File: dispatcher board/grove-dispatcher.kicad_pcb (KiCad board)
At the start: 2 copper layers, 36 parts, among them P1 CONN_01X05, P10 CONN_01X06, P11 CONN_01X06, P12 CONN_01X06, P13 CONN_01X06, P14 CONN_01X06, P15 CONN_01X06, P16 CONN_01X06, P17 CONN_01X06, P18 CONN_01X06, P19 CONN_01X06, P2 CONN_01X06, P20 CONN_01X06, P3 CONN_01X05, P4 CONN_01X05, P5 CONN_01X05, P6 CONN_01X06, P7 CONN_01X06, P8 CONN_01X06, P9 CONN_01X06, U1 PICO_BUCK, U2 PICO_BUCK, U3 PICO_BUCK, U4 PICO_BUCK

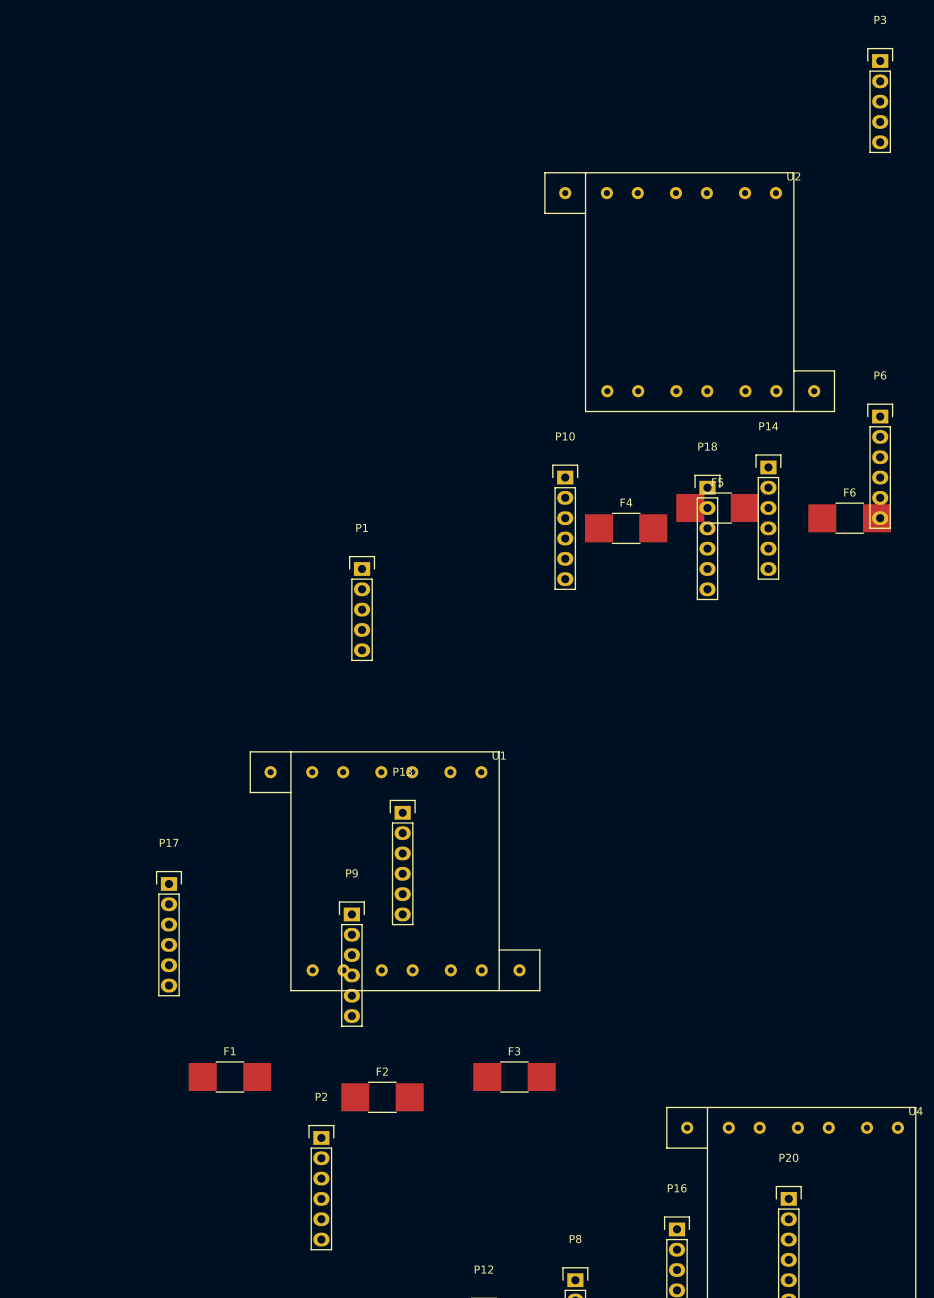
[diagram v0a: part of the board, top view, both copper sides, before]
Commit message: Some test placement on PCB
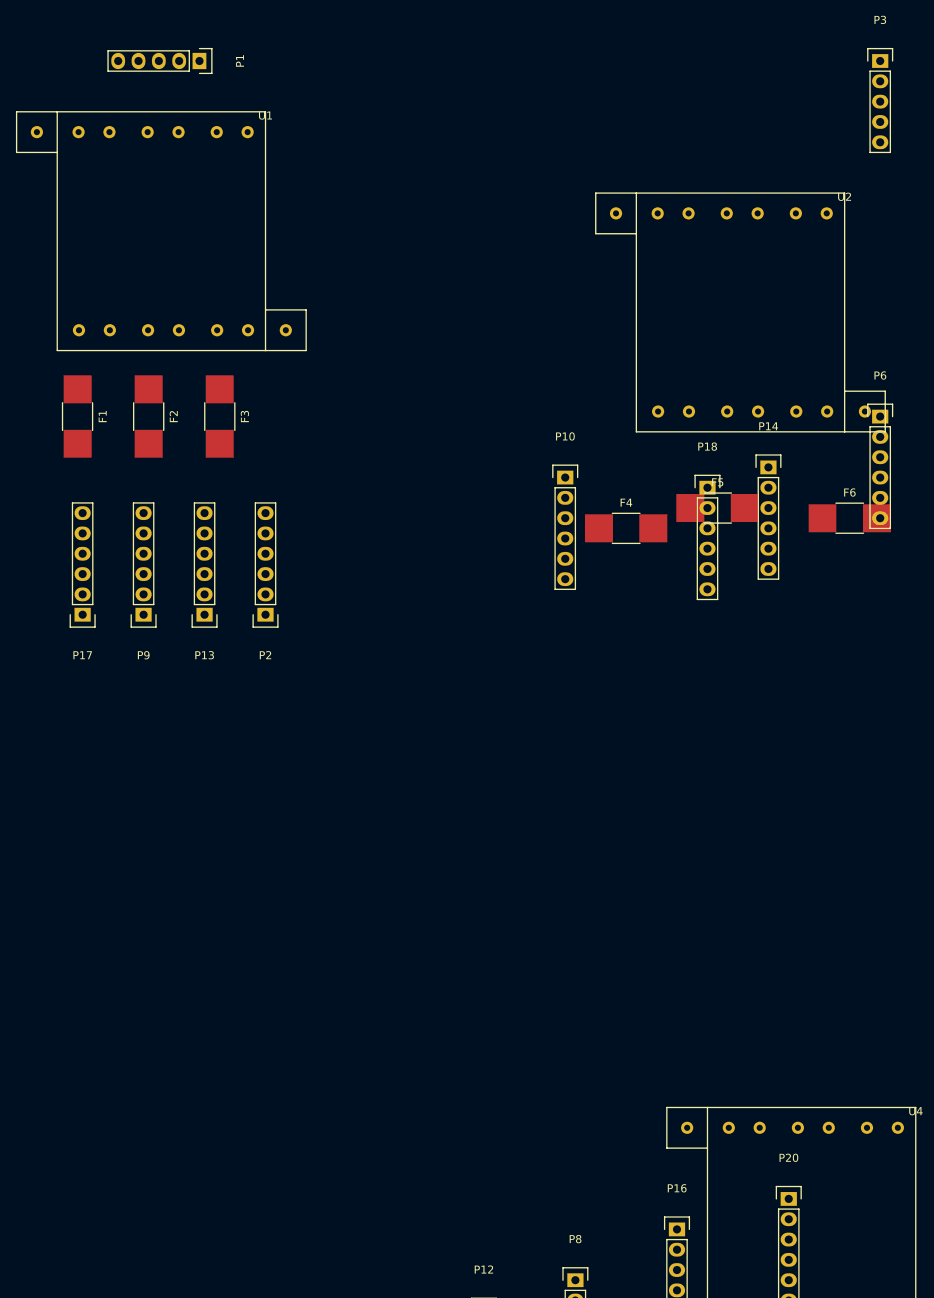
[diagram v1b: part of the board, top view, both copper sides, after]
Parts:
- moved F3 90.4 mm to (43.2, 61.0), turned to 270 degrees
- moved F2 90.0 mm to (34.3, 61.0), turned to 270 degrees
- moved U1 85.2 mm to (22.9, 22.9)
- moved F1 84.7 mm to (25.4, 61.0), turned to 270 degrees
- moved P1 66.7 mm to (40.6, 16.5), turned to 270 degrees
- moved P2 65.8 mm to (48.9, 85.7), turned to 180 degrees
- moved P9 45.6 mm to (33.7, 85.7), turned to 180 degrees
- moved P17 35.3 mm to (26.0, 85.7), turned to 180 degrees
- moved P13 35.0 mm to (41.3, 85.7), turned to 180 degrees
- moved U2 6.84 mm to (95.2, 33.0)

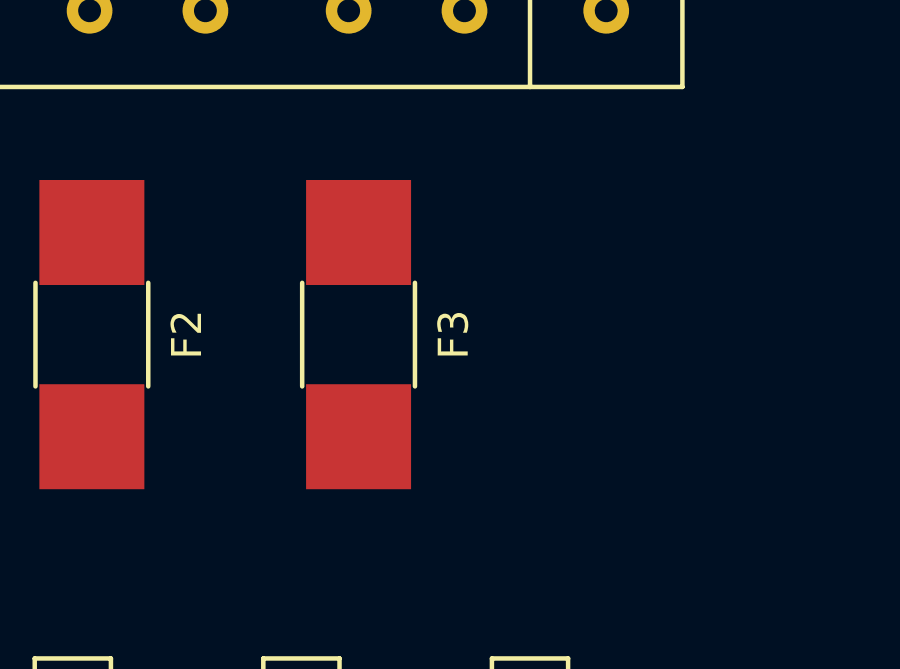
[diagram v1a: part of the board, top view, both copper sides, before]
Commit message: Some tweaks to the gitignore and pcb file
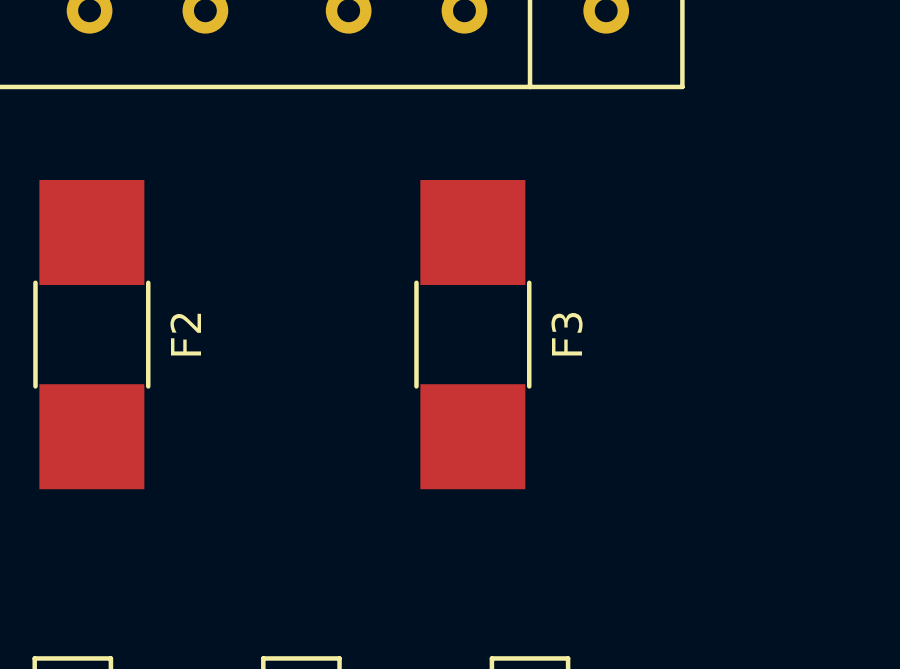
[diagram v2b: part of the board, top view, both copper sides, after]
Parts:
- moved F3 3.81 mm to (47.0, 61.0)
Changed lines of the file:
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@@
   )
   (module Resistors_SMD:R_1812_HandSoldering (layer F.Cu)
-    (at 43.18 60.96 270)
+    (at 46.99 60.96 270)
     (descr "Resistor SMD 1812, hand soldering, Panasonic (see ERJ12)")
     (tags "resistor 1812")

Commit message: First pass at routing this simple board
Conn for LED are spaced far enough apart to allow
for MTA connectors which are 0.3 inch or more thick
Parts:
- added R1: 0, Resistors_SMD:R_0805_HandSoldering, F.Cu at (119.4, 130.8)
- added R10: 0, Resistors_SMD:R_0805_HandSoldering, F.Cu at (182.2, 102.2)
- added R11: 0, Resistors_SMD:R_0805_HandSoldering, F.Cu at (182.2, 111.1)
- added R12: 0, Resistors_SMD:R_0805_HandSoldering, F.Cu at (182.2, 120.0)
- added R2: 0, Resistors_SMD:R_0805_HandSoldering, F.Cu at (119.4, 121.9)
- added R3: 0, Resistors_SMD:R_0805_HandSoldering, F.Cu at (119.4, 113.0)
- added R4: 0, Resistors_SMD:R_0805_HandSoldering, F.Cu at (119.4, 92.7)
- added R5: 0, Resistors_SMD:R_0805_HandSoldering, F.Cu at (119.4, 83.8)
- added R6: 0, Resistors_SMD:R_0805_HandSoldering, F.Cu at (119.4, 74.9)
- added R7: 0, Resistors_SMD:R_0805_HandSoldering, F.Cu at (182.2, 66.7)
- added R8: 0, Resistors_SMD:R_0805_HandSoldering, F.Cu at (182.2, 75.6)
- added R9: 0, Resistors_SMD:R_0805_HandSoldering, F.Cu at (182.2, 84.5)
- P11, P16, P6: value CONN_01X06 -> CONN_01X05; footprint Pin_Headers:Pin_Header_Straight_1x06 -> Pin_Headers:Pin_Header_Straight_1x05
- P3, P4, P5: value CONN_01X05 -> CONN_01X06; footprint Pin_Headers:Pin_Header_Straight_1x05 -> Pin_Headers:Pin_Header_Straight_1x06
- moved P16 134.2 mm to (226.7, 117.5), turned to 180 degrees
- moved U4 124.2 mm to (220.3, 103.5), turned to 270 degrees
- moved P8 123.7 mm to (169.5, 76.2), turned to 180 degrees
- moved P4 122.1 mm to (132.1, 114.3), turned to 180 degrees
- moved U1 121.6 mm to (81.3, 129.5), turned to 90 degrees
- moved F1 114.9 mm to (119.4, 127.0), turned to 0 degrees
- moved P17 111.8 mm to (132.1, 121.3), turned to 0 degrees
- moved P2 111.7 mm to (156.8, 114.3)
- moved P15 111.6 mm to (156.8, 83.2)
- moved P3 107.2 mm to (169.5, 114.3), turned to 180 degrees
- moved P12 105.5 mm to (132.1, 83.2)
- moved P13 103.5 mm to (144.8, 83.2), turned to 0 degrees
- moved F2 102.5 mm to (119.4, 118.1), turned to 0 degrees
- moved F10 100.3 mm to (182.2, 106.0), turned to 180 degrees
- moved P1 100.0 mm to (74.9, 110.5), turned to 0 degrees
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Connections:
- P1 pad 4: /V+ -> GND
- P1 pad 5: GND -> /V+
- P11 pad 1: Net-(F7-Pad2) -> Net-(P11-Pad1)
- P11 pad 3: Net-(F8-Pad2) -> Net-(P11-Pad3)
- P11 pad 4: Net-(P11-Pad4) -> GND
- P11 pad 5: Net-(F9-Pad2) -> Net-(P11-Pad5)
- P12 pad 1: Net-(F10-Pad2) -> Net-(F7-Pad2)
- P12 pad 3: Net-(F11-Pad2) -> Net-(F8-Pad2)
- P12 pad 5: Net-(F12-Pad2) -> Net-(F9-Pad2)
- P13 pad 1: Net-(F1-Pad2) -> Net-(F7-Pad2)
- P13 pad 2: Net-(P13-Pad2) -> Net-(P12-Pad2)
- P13 pad 3: Net-(F2-Pad2) -> Net-(F8-Pad2)
- P13 pad 4: Net-(P13-Pad4) -> Net-(P12-Pad4)
- P13 pad 5: Net-(F3-Pad2) -> Net-(F9-Pad2)
- P13 pad 6: Net-(P13-Pad6) -> Net-(P12-Pad6)
- P14 pad 1: Net-(F4-Pad2) -> Net-(F7-Pad2)
- P14 pad 2: Net-(P10-Pad2) -> Net-(P12-Pad2)
- P14 pad 3: Net-(F5-Pad2) -> Net-(F8-Pad2)
- P14 pad 4: Net-(P10-Pad4) -> Net-(P12-Pad4)
- P14 pad 5: Net-(F6-Pad2) -> Net-(F9-Pad2)
- P14 pad 6: Net-(P10-Pad6) -> Net-(P12-Pad6)
- P15 pad 2: Net-(P11-Pad2) -> Net-(P12-Pad2)
- P15 pad 4: Net-(P11-Pad4) -> Net-(P12-Pad4)
- P15 pad 6: Net-(P11-Pad6) -> Net-(P12-Pad6)
- P16 pad 1: Net-(F10-Pad2) -> Net-(P16-Pad1)
- P16 pad 2: Net-(P12-Pad2) -> Net-(P16-Pad2)
- P16 pad 3: Net-(F11-Pad2) -> Net-(P16-Pad3)
- P16 pad 4: Net-(P12-Pad4) -> GND
- P16 pad 5: Net-(F12-Pad2) -> Net-(P16-Pad5)
- P17 pad 1: Net-(F1-Pad2) -> Net-(F10-Pad2)
- P17 pad 2: Net-(P13-Pad2) -> Net-(P17-Pad2)
- P17 pad 3: Net-(F2-Pad2) -> Net-(F11-Pad2)
- P17 pad 4: Net-(P13-Pad4) -> Net-(P17-Pad4)
- P17 pad 5: Net-(F3-Pad2) -> Net-(F12-Pad2)
- P17 pad 6: Net-(P13-Pad6) -> Net-(P17-Pad6)
- P18 pad 1: Net-(F4-Pad2) -> Net-(F10-Pad2)
- P18 pad 2: Net-(P10-Pad2) -> Net-(P17-Pad2)
- P18 pad 3: Net-(F5-Pad2) -> Net-(F11-Pad2)
- P18 pad 4: Net-(P10-Pad4) -> Net-(P17-Pad4)
- P18 pad 5: Net-(F6-Pad2) -> Net-(F12-Pad2)
- P18 pad 6: Net-(P10-Pad6) -> Net-(P17-Pad6)
- P19 pad 1: Net-(F7-Pad2) -> Net-(F10-Pad2)
- P19 pad 2: Net-(P11-Pad2) -> Net-(P17-Pad2)
- P19 pad 3: Net-(F8-Pad2) -> Net-(F11-Pad2)
- P19 pad 4: Net-(P11-Pad4) -> Net-(P17-Pad4)
- P19 pad 5: Net-(F9-Pad2) -> Net-(F12-Pad2)
- P19 pad 6: Net-(P11-Pad6) -> Net-(P17-Pad6)
- P2 pad 2: Net-(P13-Pad2) -> Net-(P2-Pad2)
- P2 pad 4: Net-(P13-Pad4) -> Net-(P2-Pad4)
- P2 pad 6: Net-(P13-Pad6) -> Net-(P2-Pad6)
- P20 pad 2: Net-(P12-Pad2) -> Net-(P17-Pad2)
- P20 pad 4: Net-(P12-Pad4) -> Net-(P17-Pad4)
- P20 pad 6: Net-(P12-Pad6) -> Net-(P17-Pad6)
- P3 pad 1: Net-(P3-Pad1) -> Net-(F1-Pad2)
- P3 pad 2: Net-(P3-Pad2) -> Net-(P2-Pad2)
- P3 pad 3: Net-(P3-Pad3) -> Net-(F2-Pad2)
- P3 pad 4: /V+ -> Net-(P2-Pad4)
- P3 pad 5: GND -> Net-(F3-Pad2)
- P4 pad 1: Net-(P4-Pad1) -> Net-(F1-Pad2)
- P4 pad 2: Net-(P4-Pad2) -> Net-(P2-Pad2)
- P4 pad 3: Net-(P4-Pad3) -> Net-(F2-Pad2)
- P4 pad 4: /V+ -> Net-(P2-Pad4)
- P4 pad 5: GND -> Net-(F3-Pad2)
- P5 pad 1: Net-(P5-Pad1) -> Net-(F1-Pad2)
- P5 pad 2: Net-(P5-Pad2) -> Net-(P2-Pad2)
- P5 pad 3: Net-(P5-Pad3) -> Net-(F2-Pad2)
- P5 pad 4: /V+ -> Net-(P2-Pad4)
- P5 pad 5: GND -> Net-(F3-Pad2)
- P6 pad 1: Net-(F4-Pad2) -> Net-(P6-Pad1)
- P6 pad 2: Net-(P10-Pad2) -> Net-(P6-Pad2)
- P6 pad 3: Net-(F5-Pad2) -> Net-(P6-Pad3)
- P6 pad 4: Net-(P10-Pad4) -> GND
- P6 pad 5: Net-(F6-Pad2) -> Net-(P6-Pad5)
- P7 pad 1: Net-(F7-Pad2) -> Net-(F4-Pad2)
- P7 pad 2: Net-(P11-Pad2) -> Net-(P10-Pad2)
- P7 pad 3: Net-(F8-Pad2) -> Net-(F5-Pad2)
- P7 pad 4: Net-(P11-Pad4) -> Net-(P10-Pad4)
- P7 pad 5: Net-(F9-Pad2) -> Net-(F6-Pad2)
- P7 pad 6: Net-(P11-Pad6) -> Net-(P10-Pad6)
- P8 pad 1: Net-(F10-Pad2) -> Net-(F4-Pad2)
- P8 pad 2: Net-(P12-Pad2) -> Net-(P10-Pad2)
- P8 pad 3: Net-(F11-Pad2) -> Net-(F5-Pad2)
- P8 pad 4: Net-(P12-Pad4) -> Net-(P10-Pad4)
- P8 pad 5: Net-(F12-Pad2) -> Net-(F6-Pad2)
- P8 pad 6: Net-(P12-Pad6) -> Net-(P10-Pad6)
- P9 pad 1: Net-(F1-Pad2) -> Net-(F4-Pad2)
- P9 pad 2: Net-(P13-Pad2) -> Net-(P10-Pad2)
- P9 pad 3: Net-(F2-Pad2) -> Net-(F5-Pad2)
- P9 pad 4: Net-(P13-Pad4) -> Net-(P10-Pad4)
- P9 pad 5: Net-(F3-Pad2) -> Net-(F6-Pad2)
- P9 pad 6: Net-(P13-Pad6) -> Net-(P10-Pad6)
- U1 pad 0: Net-(P1-Pad3) -> Net-(P1-Pad1)
- U1 pad 11: Net-(P13-Pad6) -> Net-(P2-Pad6)
- U1 pad 2: Net-(P1-Pad1) -> Net-(P1-Pad3)
- U1 pad 7: Net-(P13-Pad2) -> Net-(P2-Pad2)
- U1 pad 9: Net-(P13-Pad4) -> Net-(P2-Pad4)
- U2 pad 0: Net-(P3-Pad3) -> Net-(P6-Pad1)
- U2 pad 1: Net-(P3-Pad2) -> Net-(P6-Pad2)
- U2 pad 2: Net-(P3-Pad1) -> Net-(P6-Pad3)
- U2 pad 5: /V+ -> Net-(P6-Pad5)
- U3 pad 0: Net-(P4-Pad3) -> Net-(P11-Pad1)
- U3 pad 1: Net-(P4-Pad2) -> Net-(P11-Pad2)
- U3 pad 11: Net-(P11-Pad6) -> Net-(P12-Pad6)
- U3 pad 2: Net-(P4-Pad1) -> Net-(P11-Pad3)
- U3 pad 5: /V+ -> Net-(P11-Pad5)
- U3 pad 7: Net-(P11-Pad2) -> Net-(P12-Pad2)
- U3 pad 9: Net-(P11-Pad4) -> Net-(P12-Pad4)
- U4 pad 0: Net-(P5-Pad3) -> Net-(P16-Pad1)
- U4 pad 1: Net-(P5-Pad2) -> Net-(P16-Pad2)
- U4 pad 11: Net-(P12-Pad6) -> Net-(P17-Pad6)
- U4 pad 2: Net-(P5-Pad1) -> Net-(P16-Pad3)
- U4 pad 5: /V+ -> Net-(P16-Pad5)
- U4 pad 7: Net-(P12-Pad2) -> Net-(P17-Pad2)
- U4 pad 9: Net-(P12-Pad4) -> Net-(P17-Pad4)
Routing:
- net Net-(P17-Pad2): track 0.00 -> 71.8 mm
- net Net-(P2-Pad2): track 0.00 -> 70.4 mm
- net Net-(P12-Pad2): track 0.00 -> 69.7 mm
- net Net-(P10-Pad2): track 0.00 -> 69.7 mm
- net Net-(P17-Pad4): track 0.00 -> 67.9 mm
- net Net-(P2-Pad4): track 0.00 -> 66.9 mm
- net Net-(P10-Pad4): track 0.00 -> 66.9 mm
- net Net-(P10-Pad6): track 0.00 -> 65.8 mm
- net Net-(P12-Pad4): track 0.00 -> 65.7 mm
- net Net-(P17-Pad6): track 0.00 -> 63.7 mm
- net Net-(P2-Pad6): track 0.00 -> 62.7 mm
- net Net-(P12-Pad6): track 0.00 -> 62.7 mm
- net Net-(F10-Pad2): track 0.00 -> 61.2 mm
- net Net-(F7-Pad2): track 0.00 -> 60.8 mm
- net Net-(F4-Pad2): track 0.00 -> 60.2 mm
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- added copper zone on F.Cu, net GND
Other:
- board outline added: 158.8 x 77.5 mm

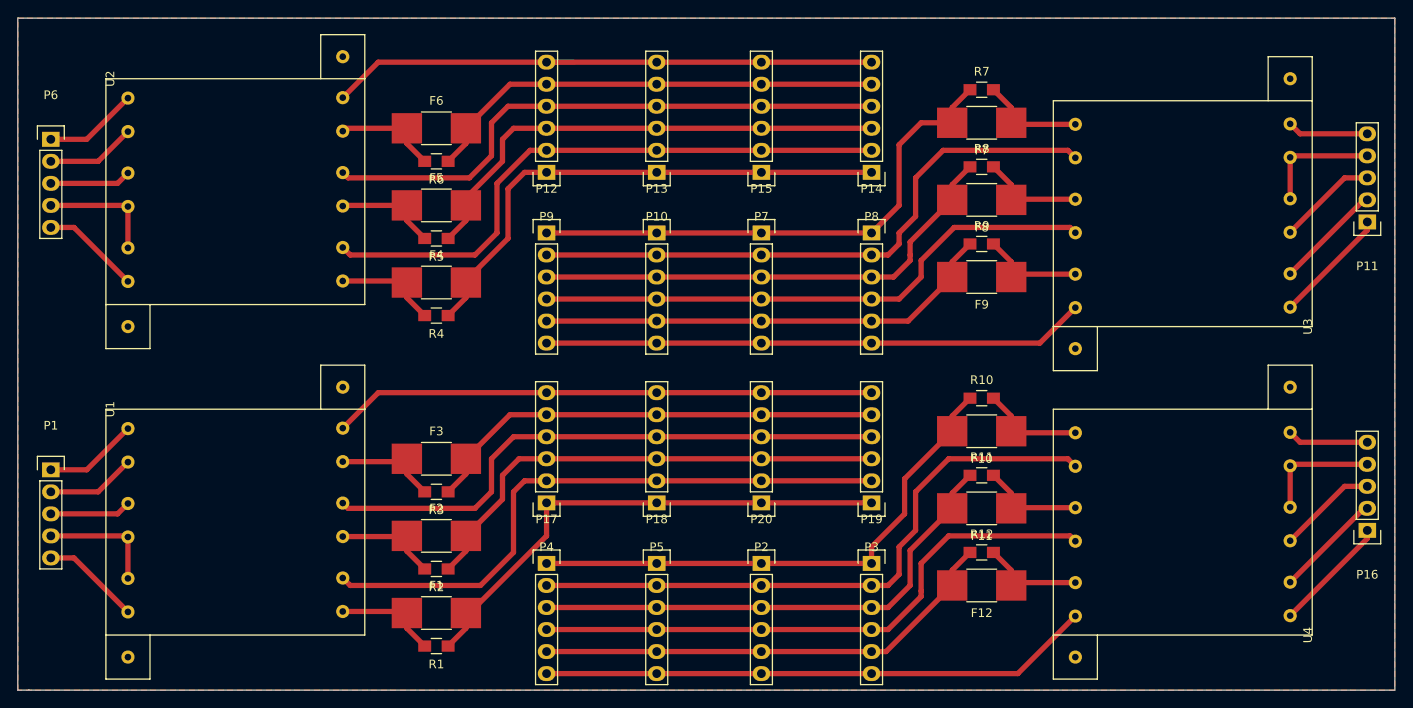
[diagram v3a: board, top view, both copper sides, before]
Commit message: Add some mounting holes
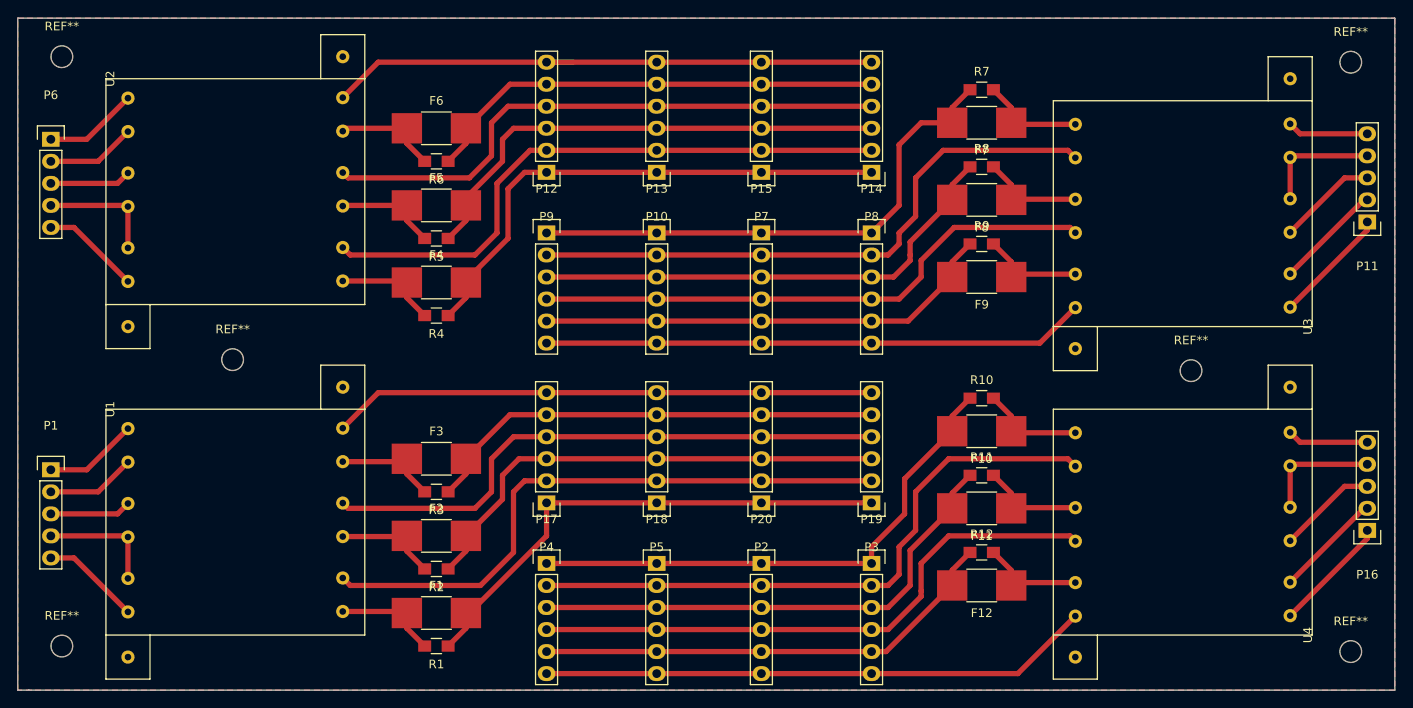
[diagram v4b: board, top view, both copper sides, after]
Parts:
- added REF**: MountingHole_2.5mm, Mounting_Holes:MountingHole_2.5mm, F.Cu at (224.8, 63.5)
- added REF**: MountingHole_2.5mm, Mounting_Holes:MountingHole_2.5mm, F.Cu at (206.4, 99.1)
- added REF**: MountingHole_2.5mm, Mounting_Holes:MountingHole_2.5mm, F.Cu at (224.8, 131.4)
- added REF**: MountingHole_2.5mm, Mounting_Holes:MountingHole_2.5mm, F.Cu at (76.2, 62.9)
- added REF**: MountingHole_2.5mm, Mounting_Holes:MountingHole_2.5mm, F.Cu at (95.9, 97.8)
- added REF**: MountingHole_2.5mm, Mounting_Holes:MountingHole_2.5mm, F.Cu at (76.2, 130.8)
